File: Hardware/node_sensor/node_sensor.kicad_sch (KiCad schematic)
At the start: 14 parts, among them J1 Conn_Jack-DC, J2 Pump, J3 Light, U1 DevKitESP32, U2 DHT11, U3 BH1750, U4 ADS1115, U5 DS3231, U6 Soil-Moisture, U7 Soil-Moisture, U8 Soil-Moisture, U9 Soil-Moisture

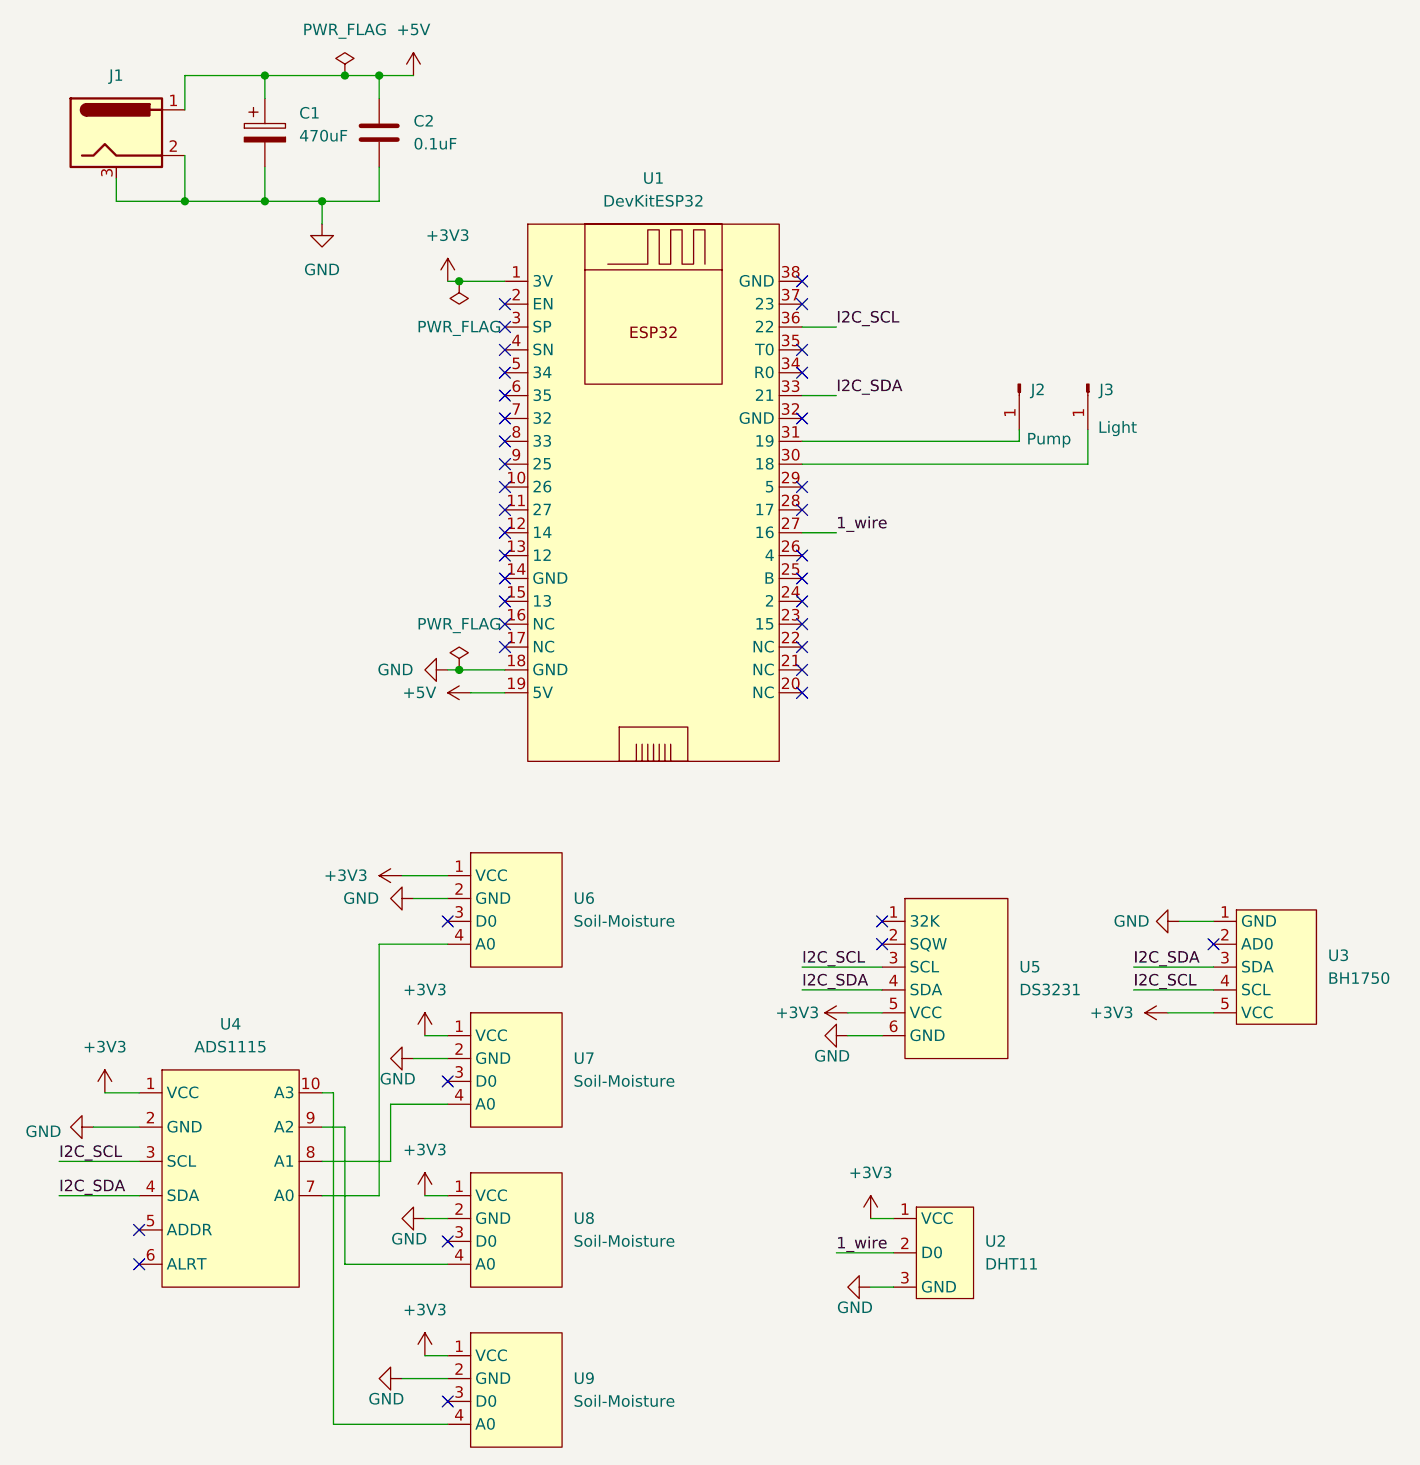
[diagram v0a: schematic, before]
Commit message: change topic - switch pi 4
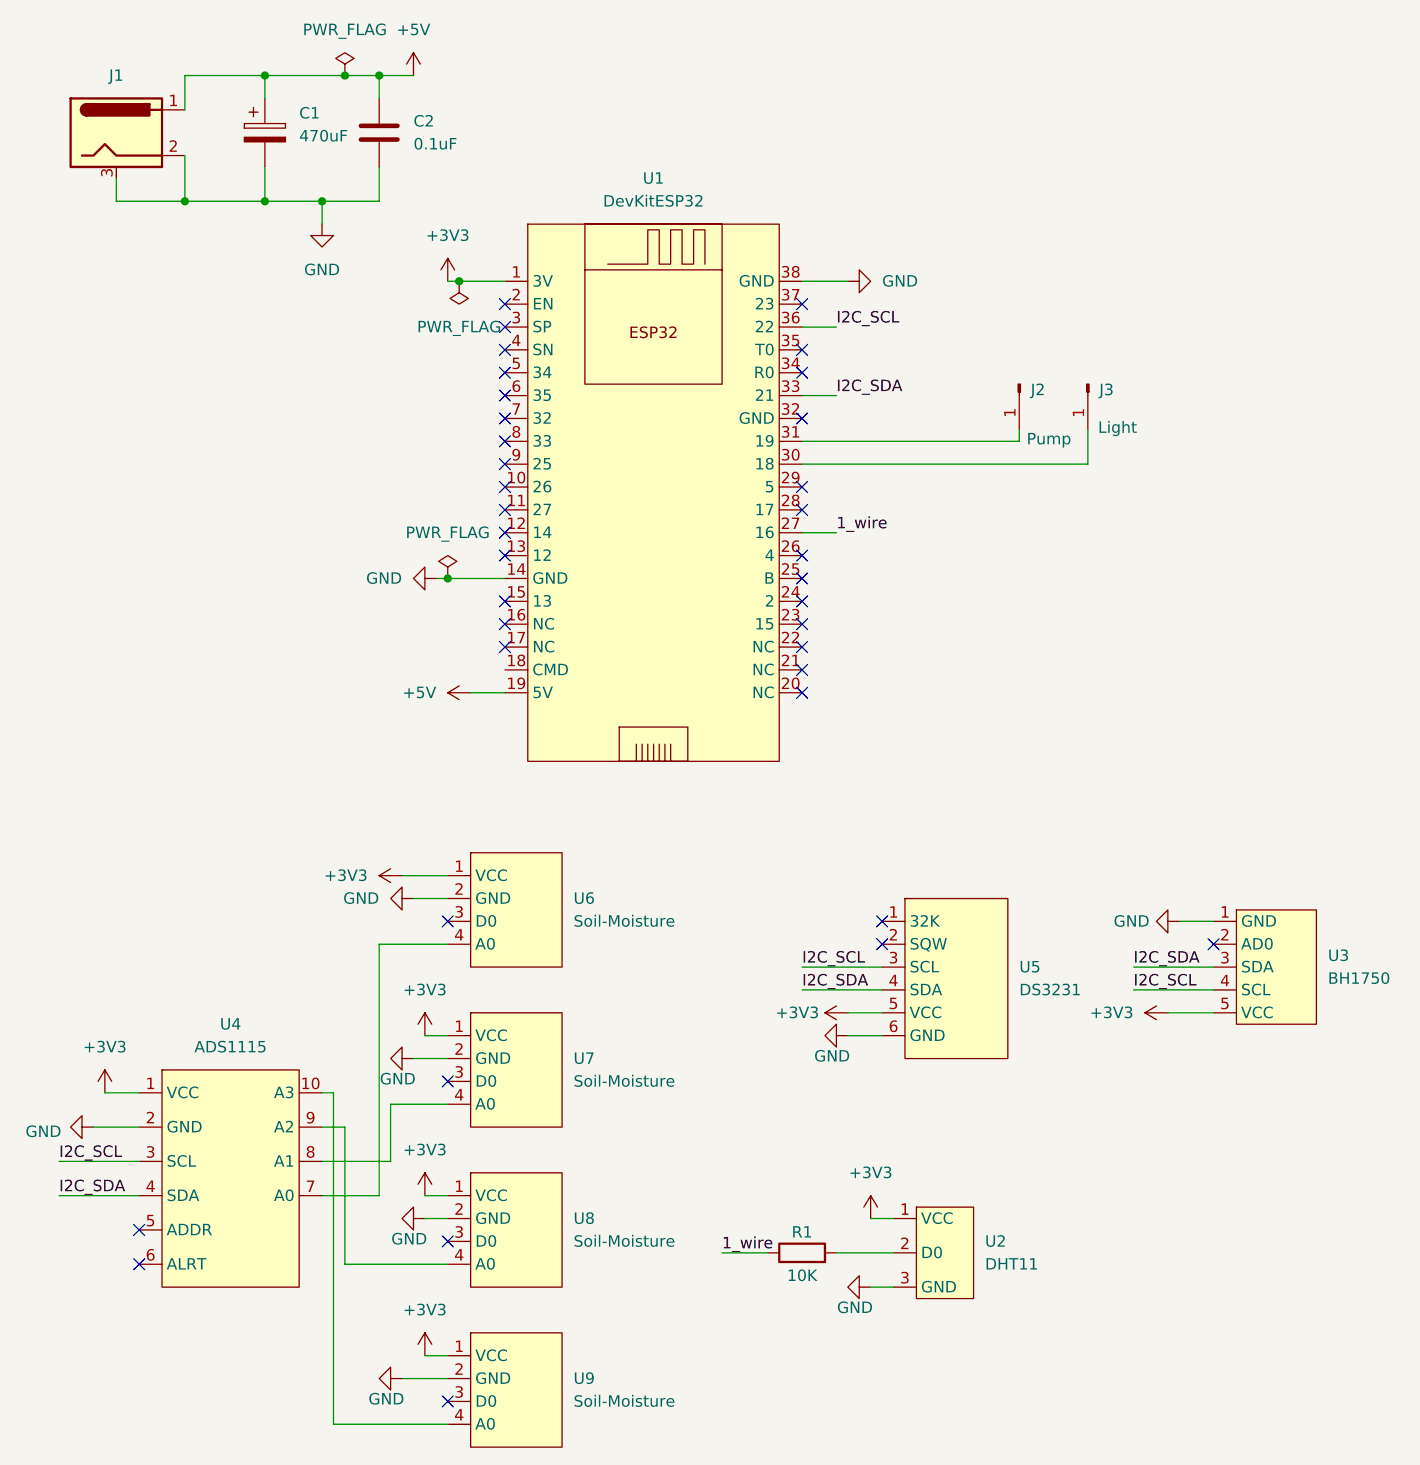
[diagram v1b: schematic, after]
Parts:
- added R1: 10K, Resistor_THT:R_Axial_DIN0207_L6.3mm_D2.5mm_P10.16mm_Horizontal, symbol Device:R
- C1: footprint MY_FOOTPRINTS:CP_Elec_6.3x7.7 -> Capacitor_THT:C_Radial_D8.0mm_H11.5mm_P3.50mm
- C2: footprint MY_FOOTPRINTS:C_0805 -> Capacitor_THT:C_Disc_D3.0mm_W1.6mm_P2.50mm
- U2: footprint Connector_PinSocket_2.54mm:PinSocket_1x03_P2.54mm_Vertical -> Connector_JST:JST_XH_B3B-XH-A_1x03_P2.50mm_Vertical
- U3: footprint Connector_PinSocket_2.54mm:PinSocket_1x05_P2.54mm_Vertical -> Connector_JST:JST_XH_B5B-XH-A_1x05_P2.50mm_Vertical
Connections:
- net 1_wire: now also R1.1; no longer U2.2 (D0)
- net GND: now also U1.14 (GND), U1.38 (GND); no longer U1.18 (GND)
- new net: R1.2, U2.2 (D0)
- no-connect marks 39 -> 37
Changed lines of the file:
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@@
 	)
 	(junction
-		(at 60.96 86.36)
+		(at 59.69 76.2)
 		(diameter 0)
 		(color 0 0 0 0)
@@
 	)
 	(no_connect
-		(at 99.06 43.18)
-	)
-	(no_connect
-		(at 66.04 76.2)
-	)
-	(no_connect
 		(at 99.06 83.82)
 	)
@@
 	(wire
 		(pts
-			(xy 59.69 86.36) (xy 60.96 86.36)
+			(xy 58.42 76.2) (xy 59.69 76.2)
 		)
 		(stroke
@@
 	(wire
 		(pts
-			(xy 60.96 86.36) (xy 66.04 86.36)
+			(xy 59.69 76.2) (xy 66.04 76.2)
 		)
 		(stroke
@@
 	(wire
 		(pts
+			(xy 99.06 43.18) (xy 104.14 43.18)
+		)
+		(stroke
+			(width 0)
+			(type default)
+		)
+	)
+	(wire
+		(pts
 			(xy 45.72 34.29) (xy 52.07 34.29)
 		)
@@
 	(wire
 		(pts
+			(xy 90.17 151.13) (xy 95.25 151.13)
+		)
+		(stroke
+			(width 0)
+			(type default)
+		)
+	)
+	(wire
+		(pts
 			(xy 104.14 127) (xy 107.95 127)
 		)
@@
 	)
 	(label "1_wire"
-		(at 102.87 151.13 0)
+		(at 90.17 151.13 0)
 		(effects
 			(font
@@
 	(symbol
 		(lib_id "power:PWR_FLAG")
-		(at 60.96 86.36 0)
+		(at 59.69 76.2 0)
 		(unit 1)
 		(body_style 1)
@@
 		(fields_autoplaced yes)
 		(property "Reference" "#FLG02"
-			(at 60.96 84.455 0)
+			(at 59.69 74.295 0)
 			(hide yes)
 			(show_name no)
@@
 		)
 		(property "Value" "PWR_FLAG"
-			(at 60.96 81.28 0)
+			(at 59.69 71.12 0)
 			(show_name no)
 			(do_not_autoplace no)
@@
 		)
 		(property "Footprint" ""
-			(at 60.96 86.36 0)
+			(at 59.69 76.2 0)
 			(hide yes)
 			(show_name no)
@@
 		)
 		(property "Datasheet" ""
-			(at 60.96 86.36 0)
+			(at 59.69 76.2 0)
 			(hide yes)
 			(show_name no)
@@
 		)
 		(property "Description" "Special symbol for telling ERC where power comes from"
-			(at 60.96 86.36 0)
+			(at 59.69 76.2 0)
 			(hide yes)
 			(show_name no)
@@
 			)
 		)
-		(property "Footprint" "Connector_PinSocket_2.54mm:PinSocket_1x03_P2.54mm_Vertical"
+		(property "Footprint" "Connector_JST:JST_XH_B3B-XH-A_1x03_P2.50mm_Vertical"
 			(at 109.22 151.13 0)
 			(hide yes)
@@
 			)
 		)
-		(property "Footprint" "Connector_PinSocket_2.54mm:PinSocket_1x05_P2.54mm_Vertical"
+		(property "Footprint" "Connector_JST:JST_XH_B5B-XH-A_1x05_P2.50mm_Vertical"
 			(at 144.78 114.3 0)
 			(hide yes)
@@
 			)
 		)
-		(property "Footprint" "MY_FOOTPRINTS:C_0805"
+		(property "Footprint" "Capacitor_THT:C_Disc_D3.0mm_W1.6mm_P2.50mm"
 			(at 53.0352 30.48 0)
 			(hide yes)
@@
 	)
 	(symbol
+		(lib_id "Device:R")
+		(at 99.06 151.13 90)
+		(unit 1)
+		(body_style 1)
+		(exclude_from_sim no)
+		(in_bom yes)
+		(on_board yes)
+		(in_pos_files yes)
+		(dnp no)
+		(property "Reference" "R1"
+			(at 99.06 148.844 90)
+			(show_name no)
+			(do_not_autoplace no)
+			(effects
+				(font
+					(size 1.27 1.27)
+				)
+			)
+		)
+		(property "Value" "10K"
+			(at 99.06 153.67 90)
+			(show_name no)
+			(do_not_autoplace no)
+			(effects
+				(font
+					(size 1.27 1.27)
+				)
+			)
+		)
+		(property "Footprint" "Resistor_THT:R_Axial_DIN0207_L6.3mm_D2.5mm_P10.16mm_Horizontal"
+			(at 99.06 152.908 90)
+			(hide yes)
+			(show_name no)
+			(do_not_autoplace no)
+			(effects
+				(font
+					(size 1.27 1.27)
+				)
+			)
+		)
+		(property "Datasheet" ""
+			(at 99.06 151.13 0)
+			(hide yes)
+			(show_name no)
+			(do_not_autoplace no)
+			(effects
+				(font
+					(size 1.27 1.27)
+				)
+			)
+		)
+		(property "Description" "Resistor"
+			(at 99.06 151.13 0)
+			(hide yes)
+			(show_name no)
+			(do_not_autoplace no)
+			(effects
+				(font
+					(size 1.27 1.27)
+				)
+			)
+		)
+		(pin "2"
+		)
+		(pin "1"
+		)
+		(instances
+			(project "node_sensor"
+				(path "/b1f2dde9-9c60-4b08-b31e-edf781363067"
+					(reference "R1")
+					(unit 1)
+				)
+			)
+		)
+	)
+	(symbol
 		(lib_id "MY_SYMBOLS:Soil-Moisture")
 		(at 59.69 143.51 0)
@@
 	(symbol
 		(lib_id "MY_SYMBOLS:GND")
-		(at 59.69 86.36 270)
+		(at 58.42 76.2 270)
 		(unit 1)
 		(body_style 1)
@@
 		(fields_autoplaced yes)
 		(property "Reference" "#PWR02"
-			(at 53.34 86.36 0)
+			(at 52.07 76.2 0)
 			(hide yes)
 			(show_name no)
@@
 		)
 		(property "Value" "GND"
-			(at 55.88 86.3599 90)
+			(at 54.61 76.1999 90)
 			(show_name no)
 			(do_not_autoplace no)
@@
 		)
 		(property "Footprint" ""
-			(at 59.69 86.36 0)
+			(at 58.42 76.2 0)
 			(hide yes)
 			(show_name no)
@@
 		)
 		(property "Datasheet" ""
-			(at 59.69 86.36 0)
+			(at 58.42 76.2 0)
 			(hide yes)
 			(show_name no)
@@
 		)
 		(property "Description" "Power symbol creates a global label with name \"GND\" , ground"
-			(at 59.69 86.36 0)
+			(at 58.42 76.2 0)
 			(hide yes)
 			(show_name no)
@@
 	)
 	(symbol
+		(lib_id "MY_SYMBOLS:GND")
+		(at 104.14 43.18 90)
+		(unit 1)
+		(body_style 1)
+		(exclude_from_sim no)
+		(in_bom yes)
+		(on_board yes)
+		(in_pos_files yes)
+		(dnp no)
+		(fields_autoplaced yes)
+		(property "Reference" "#PWR022"
+			(at 110.49 43.18 0)
+			(hide yes)
+			(show_name no)
+			(do_not_autoplace no)
+			(effects
+				(font
+					(size 1.27 1.27)
+				)
+			)
+		)
+		(property "Value" "GND"
+			(at 107.95 43.1799 90)
+			(show_name no)
+			(do_not_autoplace no)
+			(effects
+				(font
+					(size 1.27 1.27)
+				)
+				(justify right)
+			)
+		)
+		(property "Footprint" ""
+			(at 104.14 43.18 0)
+			(hide yes)
+			(show_name no)
+			(do_not_autoplace no)
+			(effects
+				(font
+					(size 1.27 1.27)
+				)
+			)
+		)
+		(property "Datasheet" ""
+			(at 104.14 43.18 0)
+			(hide yes)
+			(show_name no)
+			(do_not_autoplace no)
+			(effects
+				(font
+					(size 1.27 1.27)
+				)
+			)
+		)
+		(property "Description" "Power symbol creates a global label with name \"GND\" , ground"
+			(at 104.14 43.18 0)
+			(hide yes)
+			(show_name no)
+			(do_not_autoplace no)
+			(effects
+				(font
+					(size 1.27 1.27)
+				)
+			)
+		)
+		(pin "1"
+		)
+		(instances
+			(project "node_sensor"
+				(path "/b1f2dde9-9c60-4b08-b31e-edf781363067"
+					(reference "#PWR022")
+					(unit 1)
+				)
+			)
+		)
+	)
+	(symbol
 		(lib_id "MY_SYMBOLS:+3V3")
 		(at 57.15 162.56 0)
@@
 			)
 		)
-		(property "Footprint" "MY_FOOTPRINTS:CP_Elec_6.3x7.7"
+		(property "Footprint" "Capacitor_THT:C_Radial_D8.0mm_H11.5mm_P3.50mm"
 			(at 40.3352 30.48 0)
 			(hide yes)
